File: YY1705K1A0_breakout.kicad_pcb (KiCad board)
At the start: 2 copper layers, 34 x 53 mm, 10 parts, among them J1 CONN_7PIN, J2 FPC_12P_0.5mm

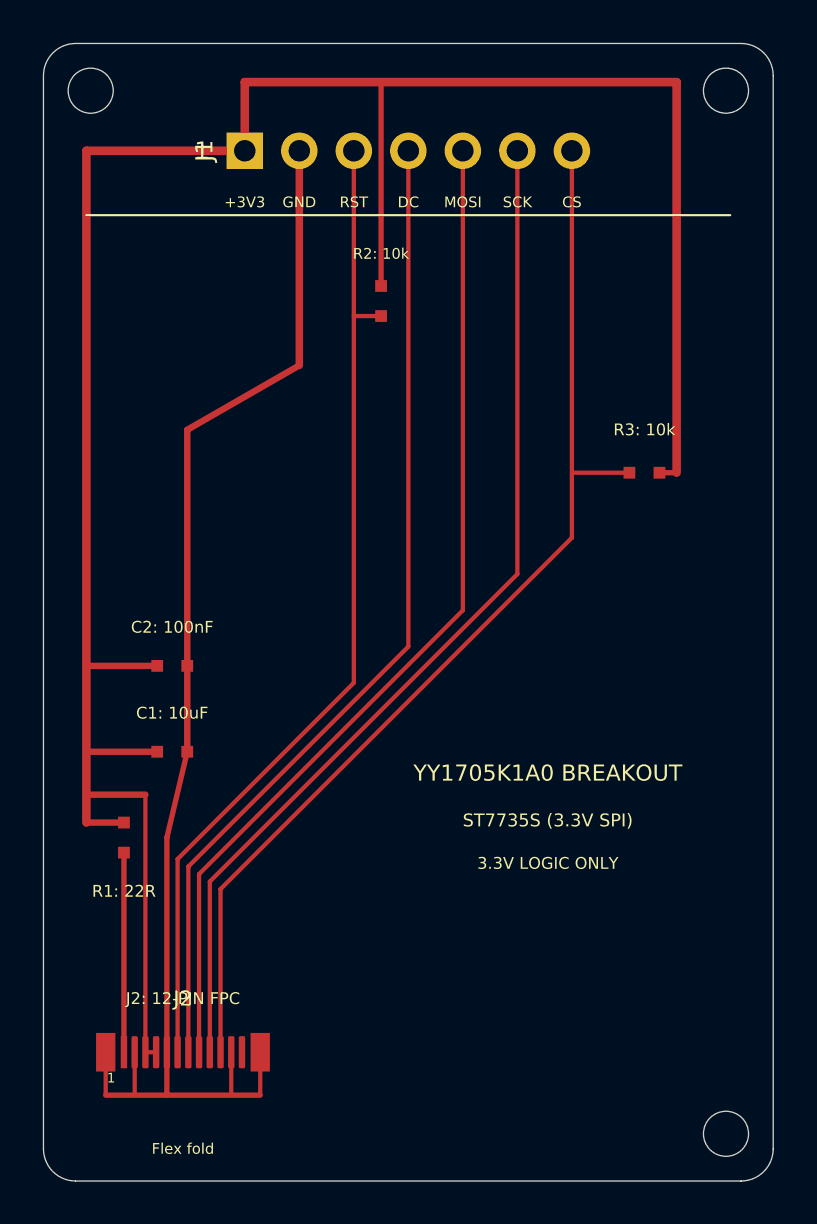
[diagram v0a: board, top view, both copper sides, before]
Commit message: Convert SMD passives to through-hole (THT)
Replace all five 0402 SMD passive components with through-hole
equivalents. Board dimensions (34x53mm) and single-layer F.Cu
constraint are preserved. J2 FPC ZIF connector remains SMD.

Component changes:
- R1 22R : SMD 0402 -> axial DIN0207 7.62mm pitch horizontal
- R2 10k : SMD 0402 -> axial DIN0207 5.08mm pitch vertical mount
- R3 10k : SMD 0402 -> axial DIN0207 5.08mm pitch vertical mount
- C1 10uF: SMD 0402 -> ceramic disc / radial THT 5mm pitch
- C2 100nF: SMD 0402 -> ceramic disc THT 5mm pitch

PCB layout:
- R2/R3 placed at Y=8.5 (just below J1) with pads landing
  directly on the RESET and CS signal traces, minimising extra routing
- C1/C2 moved to right clear-zone (X=26-32) where no signal
  diagonals pass
- R1 +3V3 routed via bottom loop (Y=51) to avoid crossing the
  five signal diagonal traces
- All routing remains single-layer F.Cu only

Files changed: kicad_pcb, kicad_sch, BOM.csv, README.md
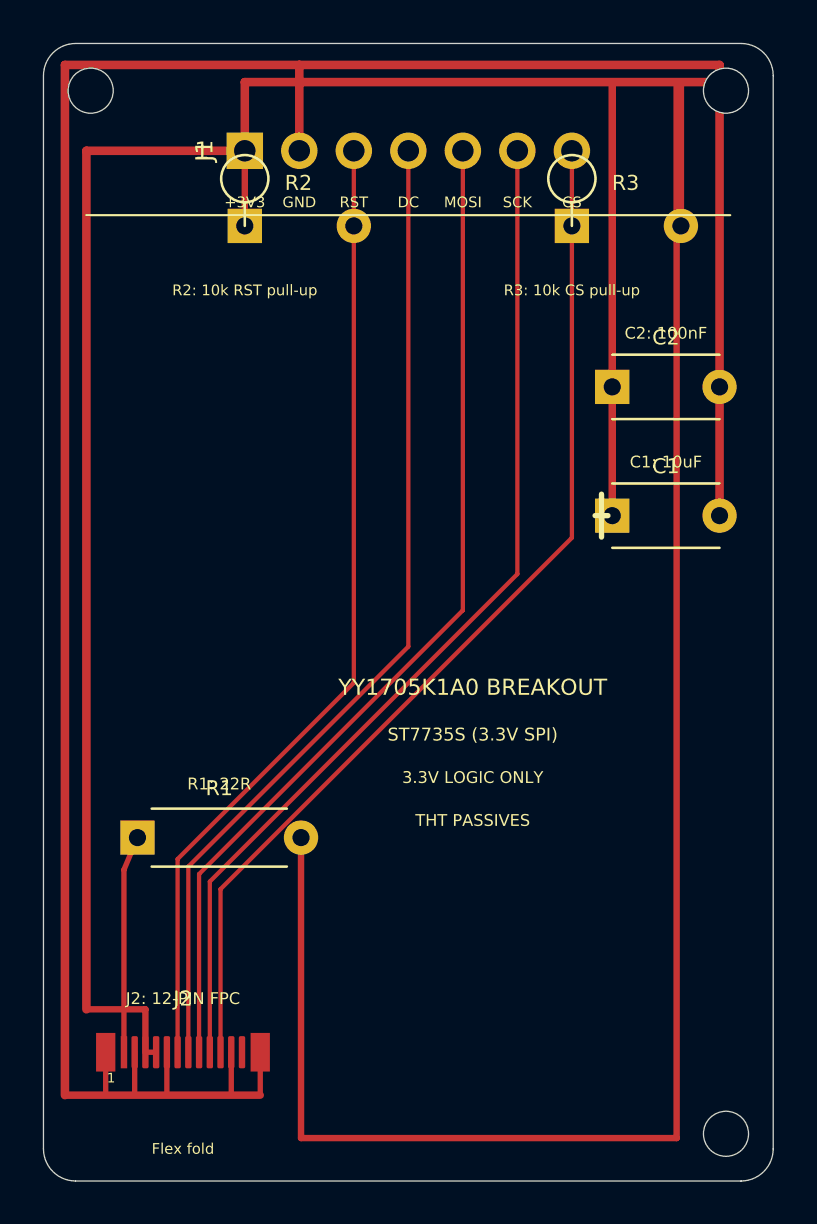
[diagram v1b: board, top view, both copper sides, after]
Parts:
- C1, C2: footprint Local:R_0402_H -> Capacitor_THT:C_Disc_D5.0mm_W2.5mm_P5.00mm
- R1: footprint Local:R_0402_V -> Resistor_THT:R_Axial_DIN0207_L6.3mm_D2.5mm_P7.62mm_Horizontal
- R2: footprint Local:R_0402_V -> Resistor_THT:R_Axial_DIN0207_L6.3mm_D2.5mm_P5.08mm_Vertical
- R3: footprint Local:R_0402_H -> Resistor_THT:R_Axial_DIN0207_L6.3mm_D2.5mm_P5.08mm_Vertical
- moved C2 26.4 mm to (29.0, 16.0)
- moved C1 25.5 mm to (29.0, 22.0)
- moved R3 12.0 mm to (24.6, 8.50)
- moved R2 7.25 mm to (9.38, 8.50)
- moved R1 4.44 mm to (8.19, 37.0)
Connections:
- R1 pad 1: +3V3 -> LEDA_SUPPLY
- R1 pad 2: LEDA_SUPPLY -> +3V3
- R2 pad 1: RESET -> +3V3
- R2 pad 2: +3V3 -> RESET
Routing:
- net +3V3: track 114.1 -> 192.2 mm
- net GND: track 62.3 -> 122.6 mm
- net CS: track 51.5 -> 48.8 mm
- net RESET: track 46.7 -> 45.4 mm
- net LEDA_SUPPLY: track 9.30 -> 10.1 mm
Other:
- board text added: "R2: 10k RST pull-up"
- board text added: "R3: 10k CS pull-up"
- board text added: "THT PASSIVES"
- board text removed: "R2: 10k"
- board text removed: "R3: 10k"
